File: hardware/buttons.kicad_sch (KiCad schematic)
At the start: 0 parts

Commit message: değişiklik yapıldı
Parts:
- added C? (x3): 100nf, symbol Device:C
- added R? (x3): 10k, symbol Device:R
- added SW? (x3): SW_Push_Open, symbol Switch:SW_Push_Open
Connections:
- new net +3.3V: R?.1, R?.1, R?.1
- new net BTN_IO: C?.1, R?.2, SW?.2 (B)
- new net BTN_MODE: C?.1, R?.2, SW?.2 (B)
- new net BTN_START: C?.1, R?.2, SW?.2 (B)
- new net GND: C?.2, C?.2, C?.2, SW?.1 (A), SW?.1 (A), SW?.1 (A)

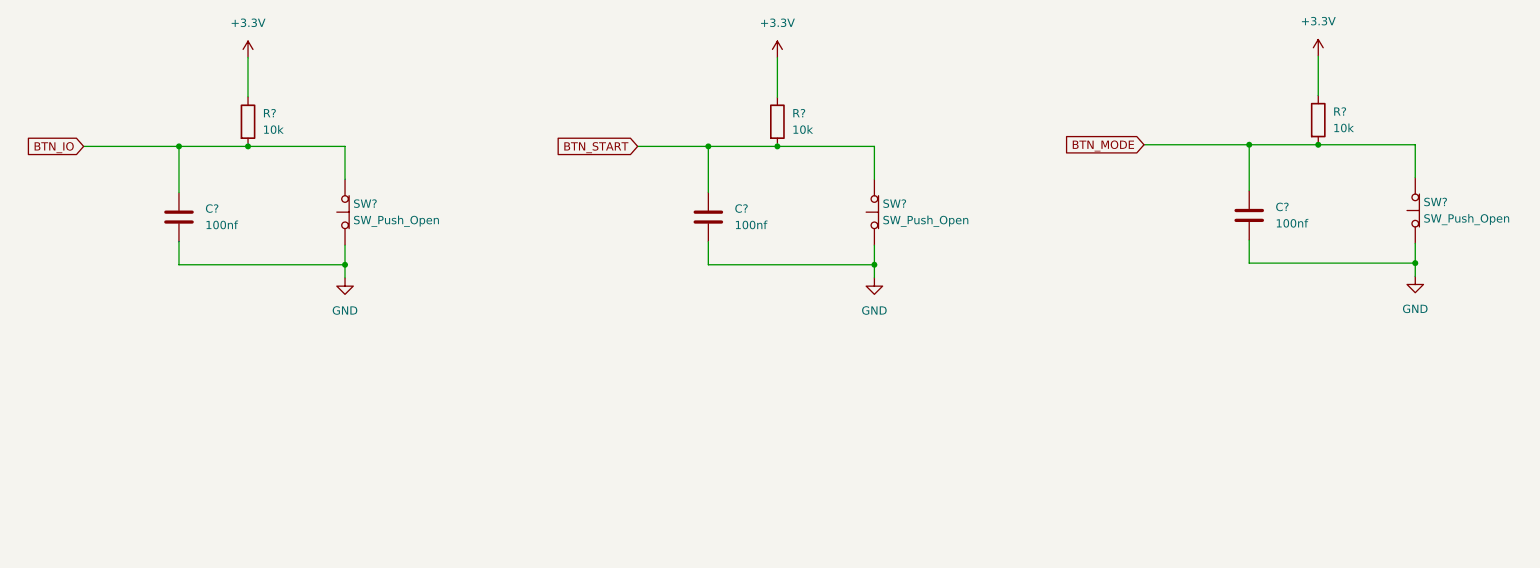
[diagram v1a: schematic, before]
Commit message: Relay module completed
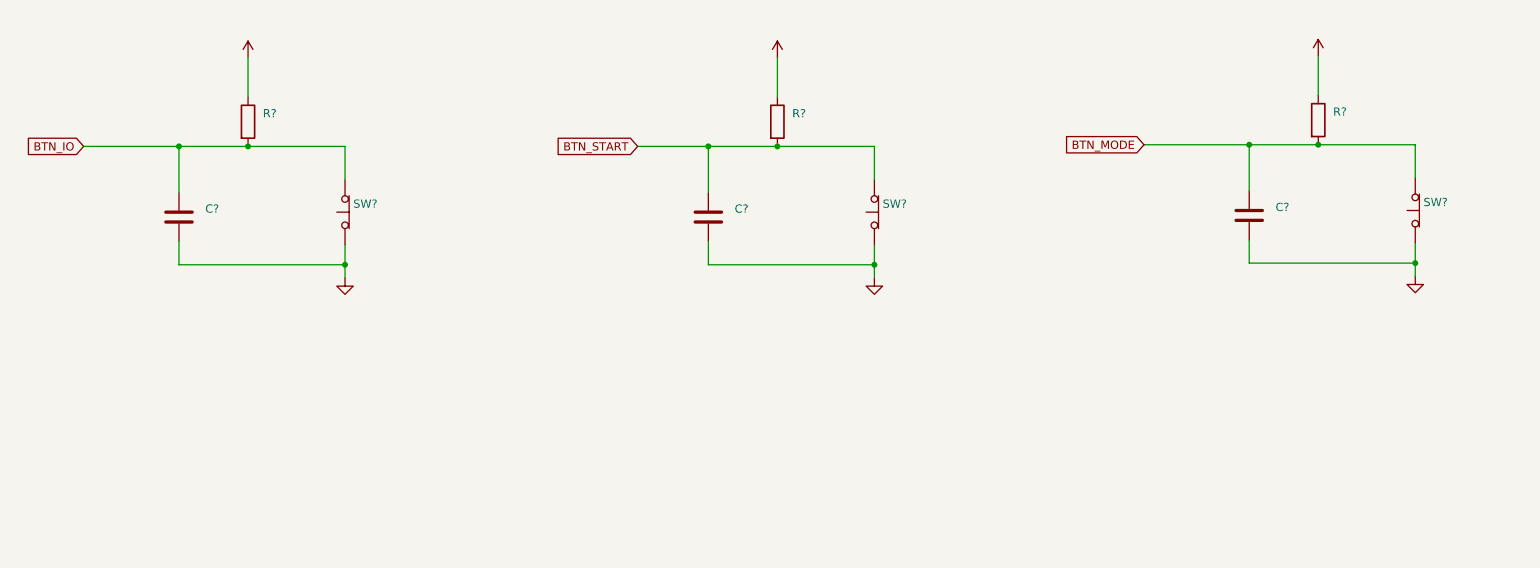
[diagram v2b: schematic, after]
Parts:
- C? (x3): value 100nf -> (none)
- R? (x3): value 10k -> (none)
- SW? (x3): value SW_Push_Open -> (none)
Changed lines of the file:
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@@
       (effects (font (size 1.27 1.27)) (justify right))
     )
-    (property "Value" "SW_Push_Open" (id 1) (at 159.258 62.2299 90)
+    (property "Value" "" (id 1) (at 159.258 62.2299 90)
       (effects (font (size 1.27 1.27)) (justify right))
     )
@@
       (effects (font (size 1.27 1.27)) (justify left))
     )
-    (property "Value" "100nf" (id 1) (at 136.398 62.9919 0)
+    (property "Value" "" (id 1) (at 136.398 62.9919 0)
       (effects (font (size 1.27 1.27)) (justify left))
     )
@@
       (effects (font (size 1.27 1.27)) (justify right))
     )
-    (property "Value" "SW_Push_Open" (id 1) (at 242.824 61.9759 90)
+    (property "Value" "" (id 1) (at 242.824 61.9759 90)
       (effects (font (size 1.27 1.27)) (justify right))
     )
@@
       (effects (font (size 1.27 1.27)) hide)
     )
-    (property "Value" "+3.3V" (id 1) (at 143.002 31.75 0))
+    (property "Value" "" (id 1) (at 143.002 31.75 0))
     (property "Footprint" "" (id 2) (at 143.002 37.084 0)
       (effects (font (size 1.27 1.27)) hide)
@@
       (effects (font (size 1.27 1.27)) hide)
     )
-    (property "Value" "GND" (id 1) (at 241.554 75.946 0))
+    (property "Value" "" (id 1) (at 241.554 75.946 0))
     (property "Footprint" "" (id 2) (at 241.554 70.866 0)
       (effects (font (size 1.27 1.27)) hide)
@@
       (effects (font (size 1.27 1.27)) (justify left))
     )
-    (property "Value" "10k" (id 1) (at 145.288 48.2599 0)
+    (property "Value" "" (id 1) (at 145.288 48.2599 0)
       (effects (font (size 1.27 1.27)) (justify left))
     )
@@
       (effects (font (size 1.27 1.27)) hide)
     )
-    (property "Value" "GND" (id 1) (at 76.2 76.2 0))
+    (property "Value" "" (id 1) (at 76.2 76.2 0))
     (property "Footprint" "" (id 2) (at 76.2 71.12 0)
       (effects (font (size 1.27 1.27)) hide)
@@
       (effects (font (size 1.27 1.27)) (justify left))
     )
-    (property "Value" "100nf" (id 1) (at 219.964 62.7379 0)
+    (property "Value" "" (id 1) (at 219.964 62.7379 0)
       (effects (font (size 1.27 1.27)) (justify left))
     )
@@
       (effects (font (size 1.27 1.27)) hide)
     )
-    (property "Value" "GND" (id 1) (at 157.988 76.2 0))
+    (property "Value" "" (id 1) (at 157.988 76.2 0))
     (property "Footprint" "" (id 2) (at 157.988 71.12 0)
       (effects (font (size 1.27 1.27)) hide)
@@
       (effects (font (size 1.27 1.27)) (justify left))
     )
-    (property "Value" "100nf" (id 1) (at 54.61 62.9919 0)
+    (property "Value" "" (id 1) (at 54.61 62.9919 0)
       (effects (font (size 1.27 1.27)) (justify left))
     )
@@
       (effects (font (size 1.27 1.27)) hide)
     )
-    (property "Value" "+3.3V" (id 1) (at 226.568 31.496 0))
+    (property "Value" "" (id 1) (at 226.568 31.496 0))
     (property "Footprint" "" (id 2) (at 226.568 36.83 0)
       (effects (font (size 1.27 1.27)) hide)
@@
       (effects (font (size 1.27 1.27)) (justify left))
     )
-    (property "Value" "10k" (id 1) (at 228.854 48.0059 0)
+    (property "Value" "" (id 1) (at 228.854 48.0059 0)
       (effects (font (size 1.27 1.27)) (justify left))
     )
@@
       (effects (font (size 1.27 1.27)) (justify left))
     )
-    (property "Value" "10k" (id 1) (at 63.5 48.2599 0)
+    (property "Value" "" (id 1) (at 63.5 48.2599 0)
       (effects (font (size 1.27 1.27)) (justify left))
     )
@@
       (effects (font (size 1.27 1.27)) (justify right))
     )
-    (property "Value" "SW_Push_Open" (id 1) (at 77.47 62.2299 90)
+    (property "Value" "" (id 1) (at 77.47 62.2299 90)
       (effects (font (size 1.27 1.27)) (justify right))
     )
@@
       (effects (font (size 1.27 1.27)) hide)
     )
-    (property "Value" "+3.3V" (id 1) (at 61.214 31.75 0))
+    (property "Value" "" (id 1) (at 61.214 31.75 0))
     (property "Footprint" "" (id 2) (at 61.214 37.084 0)
       (effects (font (size 1.27 1.27)) hide)

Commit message: Display circuit added
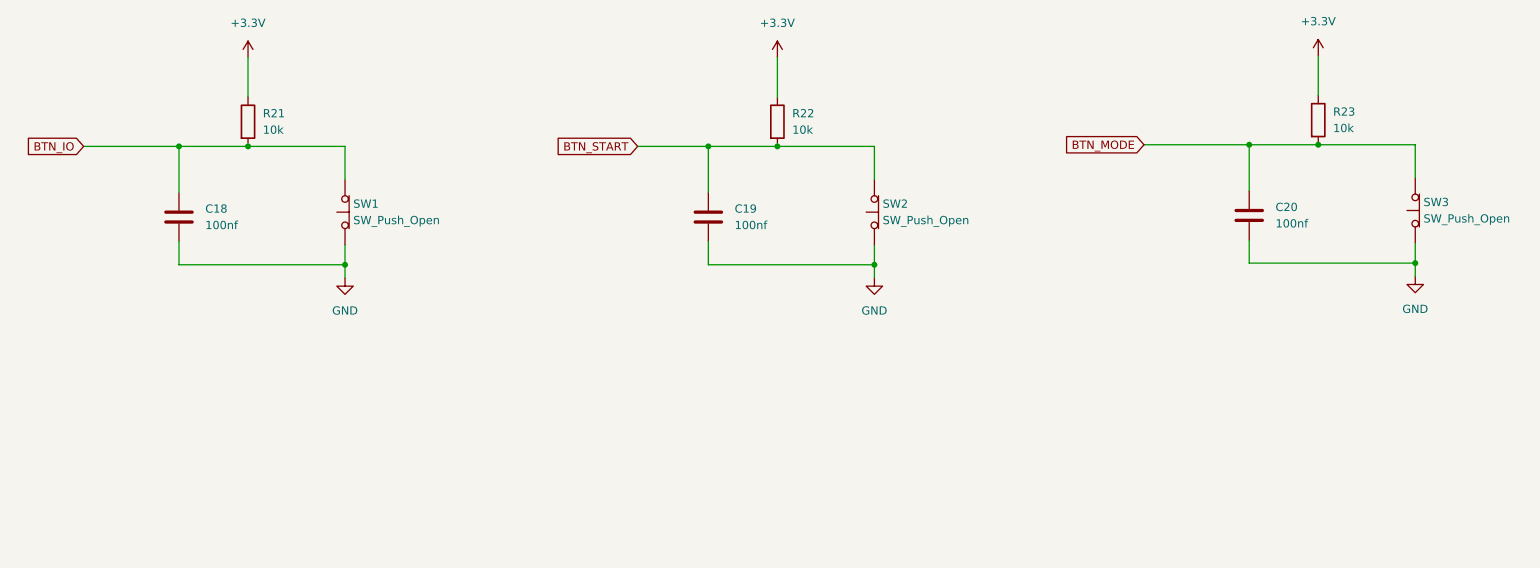
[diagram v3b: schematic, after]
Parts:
- C18, C19, C20: renamed from C?; value (none) -> 100nf
- R21, R22, R23: renamed from R?; value (none) -> 10k
- SW1, SW2, SW3: renamed from SW?; value (none) -> SW_Push_Open
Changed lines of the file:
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@@
   (symbol (lib_id "Switch:SW_Push_Open") (at 157.988 60.96 90) (unit 1)
     (in_bom yes) (on_board yes) (fields_autoplaced)
-    (property "Reference" "SW?" (id 0) (at 159.258 59.6899 90)
-      (effects (font (size 1.27 1.27)) (justify right))
-    )
-    (property "Value" "" (id 1) (at 159.258 62.2299 90)
+    (property "Reference" "SW2" (id 0) (at 159.258 59.6899 90)
+      (effects (font (size 1.27 1.27)) (justify right))
+    )
+    (property "Value" "SW_Push_Open" (id 1) (at 159.258 62.2299 90)
       (effects (font (size 1.27 1.27)) (justify right))
     )
@@
   (symbol (lib_id "Device:C") (at 132.334 61.722 0) (unit 1)
     (in_bom yes) (on_board yes) (fields_autoplaced)
-    (property "Reference" "C?" (id 0) (at 136.398 60.4519 0)
-      (effects (font (size 1.27 1.27)) (justify left))
-    )
-    (property "Value" "" (id 1) (at 136.398 62.9919 0)
+    (property "Reference" "C19" (id 0) (at 136.398 60.4519 0)
+      (effects (font (size 1.27 1.27)) (justify left))
+    )
+    (property "Value" "100nf" (id 1) (at 136.398 62.9919 0)
       (effects (font (size 1.27 1.27)) (justify left))
     )
@@
   (symbol (lib_id "Switch:SW_Push_Open") (at 241.554 60.706 90) (unit 1)
     (in_bom yes) (on_board yes) (fields_autoplaced)
-    (property "Reference" "SW?" (id 0) (at 242.824 59.4359 90)
-      (effects (font (size 1.27 1.27)) (justify right))
-    )
-    (property "Value" "" (id 1) (at 242.824 61.9759 90)
+    (property "Reference" "SW3" (id 0) (at 242.824 59.4359 90)
+      (effects (font (size 1.27 1.27)) (justify right))
+    )
+    (property "Value" "SW_Push_Open" (id 1) (at 242.824 61.9759 90)
       (effects (font (size 1.27 1.27)) (justify right))
     )
@@
   (symbol (lib_id "power:+3.3V") (at 143.002 37.084 0) (unit 1)
     (in_bom yes) (on_board yes) (fields_autoplaced)
-    (property "Reference" "#PWR?" (id 0) (at 143.002 40.894 0)
-      (effects (font (size 1.27 1.27)) hide)
-    )
-    (property "Value" "" (id 1) (at 143.002 31.75 0))
+    (property "Reference" "#PWR027" (id 0) (at 143.002 40.894 0)
+      (effects (font (size 1.27 1.27)) hide)
+    )
+    (property "Value" "+3.3V" (id 1) (at 143.002 31.75 0))
     (property "Footprint" "" (id 2) (at 143.002 37.084 0)
       (effects (font (size 1.27 1.27)) hide)
@@
   (symbol (lib_id "power:GND") (at 241.554 70.866 0) (unit 1)
     (in_bom yes) (on_board yes) (fields_autoplaced)
-    (property "Reference" "#PWR?" (id 0) (at 241.554 77.216 0)
-      (effects (font (size 1.27 1.27)) hide)
-    )
-    (property "Value" "" (id 1) (at 241.554 75.946 0))
+    (property "Reference" "#PWR030" (id 0) (at 241.554 77.216 0)
+      (effects (font (size 1.27 1.27)) hide)
+    )
+    (property "Value" "GND" (id 1) (at 241.554 75.946 0))
     (property "Footprint" "" (id 2) (at 241.554 70.866 0)
       (effects (font (size 1.27 1.27)) hide)
@@
   (symbol (lib_id "Device:R") (at 143.002 46.99 0) (unit 1)
     (in_bom yes) (on_board yes) (fields_autoplaced)
-    (property "Reference" "R?" (id 0) (at 145.288 45.7199 0)
-      (effects (font (size 1.27 1.27)) (justify left))
-    )
-    (property "Value" "" (id 1) (at 145.288 48.2599 0)
+    (property "Reference" "R22" (id 0) (at 145.288 45.7199 0)
+      (effects (font (size 1.27 1.27)) (justify left))
+    )
+    (property "Value" "10k" (id 1) (at 145.288 48.2599 0)
       (effects (font (size 1.27 1.27)) (justify left))
     )
@@
   (symbol (lib_id "power:GND") (at 76.2 71.12 0) (unit 1)
     (in_bom yes) (on_board yes) (fields_autoplaced)
-    (property "Reference" "#PWR?" (id 0) (at 76.2 77.47 0)
-      (effects (font (size 1.27 1.27)) hide)
-    )
-    (property "Value" "" (id 1) (at 76.2 76.2 0))
+    (property "Reference" "#PWR026" (id 0) (at 76.2 77.47 0)
+      (effects (font (size 1.27 1.27)) hide)
+    )
+    (property "Value" "GND" (id 1) (at 76.2 76.2 0))
     (property "Footprint" "" (id 2) (at 76.2 71.12 0)
       (effects (font (size 1.27 1.27)) hide)
@@
   (symbol (lib_id "Device:C") (at 215.9 61.468 0) (unit 1)
     (in_bom yes) (on_board yes) (fields_autoplaced)
-    (property "Reference" "C?" (id 0) (at 219.964 60.1979 0)
-      (effects (font (size 1.27 1.27)) (justify left))
-    )
-    (property "Value" "" (id 1) (at 219.964 62.7379 0)
+    (property "Reference" "C20" (id 0) (at 219.964 60.1979 0)
+      (effects (font (size 1.27 1.27)) (justify left))
+    )
+    (property "Value" "100nf" (id 1) (at 219.964 62.7379 0)
       (effects (font (size 1.27 1.27)) (justify left))
     )
@@
   (symbol (lib_id "power:GND") (at 157.988 71.12 0) (unit 1)
     (in_bom yes) (on_board yes) (fields_autoplaced)
-    (property "Reference" "#PWR?" (id 0) (at 157.988 77.47 0)
-      (effects (font (size 1.27 1.27)) hide)
-    )
-    (property "Value" "" (id 1) (at 157.988 76.2 0))
+    (property "Reference" "#PWR028" (id 0) (at 157.988 77.47 0)
+      (effects (font (size 1.27 1.27)) hide)
+    )
+    (property "Value" "GND" (id 1) (at 157.988 76.2 0))
     (property "Footprint" "" (id 2) (at 157.988 71.12 0)
       (effects (font (size 1.27 1.27)) hide)
@@
   (symbol (lib_id "Device:C") (at 50.546 61.722 0) (unit 1)
     (in_bom yes) (on_board yes) (fields_autoplaced)
-    (property "Reference" "C?" (id 0) (at 54.61 60.4519 0)
-      (effects (font (size 1.27 1.27)) (justify left))
-    )
-    (property "Value" "" (id 1) (at 54.61 62.9919 0)
+    (property "Reference" "C18" (id 0) (at 54.61 60.4519 0)
+      (effects (font (size 1.27 1.27)) (justify left))
+    )
+    (property "Value" "100nf" (id 1) (at 54.61 62.9919 0)
       (effects (font (size 1.27 1.27)) (justify left))
     )
@@
   (symbol (lib_id "power:+3.3V") (at 226.568 36.83 0) (unit 1)
     (in_bom yes) (on_board yes) (fields_autoplaced)
-    (property "Reference" "#PWR?" (id 0) (at 226.568 40.64 0)
-      (effects (font (size 1.27 1.27)) hide)
-    )
-    (property "Value" "" (id 1) (at 226.568 31.496 0))
+    (property "Reference" "#PWR029" (id 0) (at 226.568 40.64 0)
+      (effects (font (size 1.27 1.27)) hide)
+    )
+    (property "Value" "+3.3V" (id 1) (at 226.568 31.496 0))
     (property "Footprint" "" (id 2) (at 226.568 36.83 0)
       (effects (font (size 1.27 1.27)) hide)
@@
   (symbol (lib_id "Device:R") (at 226.568 46.736 0) (unit 1)
     (in_bom yes) (on_board yes) (fields_autoplaced)
-    (property "Reference" "R?" (id 0) (at 228.854 45.4659 0)
-      (effects (font (size 1.27 1.27)) (justify left))
-    )
-    (property "Value" "" (id 1) (at 228.854 48.0059 0)
+    (property "Reference" "R23" (id 0) (at 228.854 45.4659 0)
+      (effects (font (size 1.27 1.27)) (justify left))
+    )
+    (property "Value" "10k" (id 1) (at 228.854 48.0059 0)
       (effects (font (size 1.27 1.27)) (justify left))
     )
@@
   (symbol (lib_id "Device:R") (at 61.214 46.99 0) (unit 1)
     (in_bom yes) (on_board yes) (fields_autoplaced)
-    (property "Reference" "R?" (id 0) (at 63.5 45.7199 0)
-      (effects (font (size 1.27 1.27)) (justify left))
-    )
-    (property "Value" "" (id 1) (at 63.5 48.2599 0)
+    (property "Reference" "R21" (id 0) (at 63.5 45.7199 0)
+      (effects (font (size 1.27 1.27)) (justify left))
+    )
+    (property "Value" "10k" (id 1) (at 63.5 48.2599 0)
       (effects (font (size 1.27 1.27)) (justify left))
     )
@@
   (symbol (lib_id "Switch:SW_Push_Open") (at 76.2 60.96 90) (unit 1)
     (in_bom yes) (on_board yes) (fields_autoplaced)
-    (property "Reference" "SW?" (id 0) (at 77.47 59.6899 90)
-      (effects (font (size 1.27 1.27)) (justify right))
-    )
-    (property "Value" "" (id 1) (at 77.47 62.2299 90)
+    (property "Reference" "SW1" (id 0) (at 77.47 59.6899 90)
+      (effects (font (size 1.27 1.27)) (justify right))
+    )
+    (property "Value" "SW_Push_Open" (id 1) (at 77.47 62.2299 90)
       (effects (font (size 1.27 1.27)) (justify right))
     )
@@
   (symbol (lib_id "power:+3.3V") (at 61.214 37.084 0) (unit 1)
     (in_bom yes) (on_board yes) (fields_autoplaced)
-    (property "Reference" "#PWR?" (id 0) (at 61.214 40.894 0)
-      (effects (font (size 1.27 1.27)) hide)
-    )
-    (property "Value" "" (id 1) (at 61.214 31.75 0))
+    (property "Reference" "#PWR025" (id 0) (at 61.214 40.894 0)
+      (effects (font (size 1.27 1.27)) hide)
+    )
+    (property "Value" "+3.3V" (id 1) (at 61.214 31.75 0))
     (property "Footprint" "" (id 2) (at 61.214 37.084 0)
       (effects (font (size 1.27 1.27)) hide)

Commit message: Flow module completed
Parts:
- removed C18, C19, C20: 100nf, symbol Device:C
- removed R21, R22, R23: 10k, symbol Device:R
- removed SW1, SW2, SW3: SW_Push_Open, symbol Switch:SW_Push_Open
- added C? (x3): 100nF, symbol Device:C_Small
- added R? (x3): 10K, symbol Device:R_Small
- added SW?: SW_START, symbol Switch:SW_Push
- added SW?: SW_MODE, symbol Switch:SW_Push
- added SW?: SW_IO, symbol Switch:SW_Push
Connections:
- net +3.3V: now also R?.1, R?.1, R?.1
- net BTN_IO: now also C?.1, R?.2, SW?.2
- net BTN_MODE: now also C?.1, R?.2, SW?.2
- net BTN_START: now also C?.1, R?.2, SW?.2
- net GND: now also C?.2, C?.2, C?.2, SW?.1, SW?.1, SW?.1
